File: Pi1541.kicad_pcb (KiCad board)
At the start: 2 copper layers, 56.5 x 65 mm, 25 parts, among them J2 DIN, J3 OLED, Q1 BSS138, Q2 BSS138, Q3 BSS138, Q4 BSS138, U1 74LS06

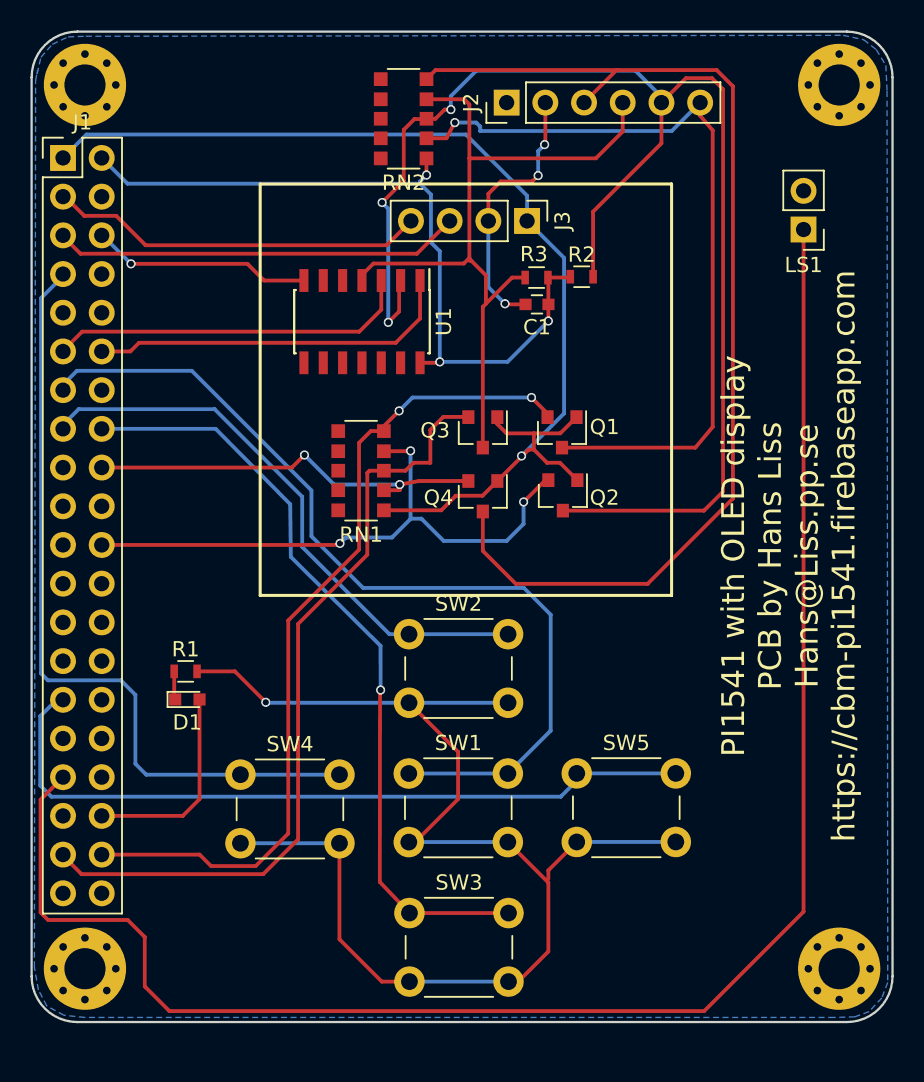
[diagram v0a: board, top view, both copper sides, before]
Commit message: Rearranged everything to correct errors Changed the buzzer footprint Replaced resistor nets with individual resistors
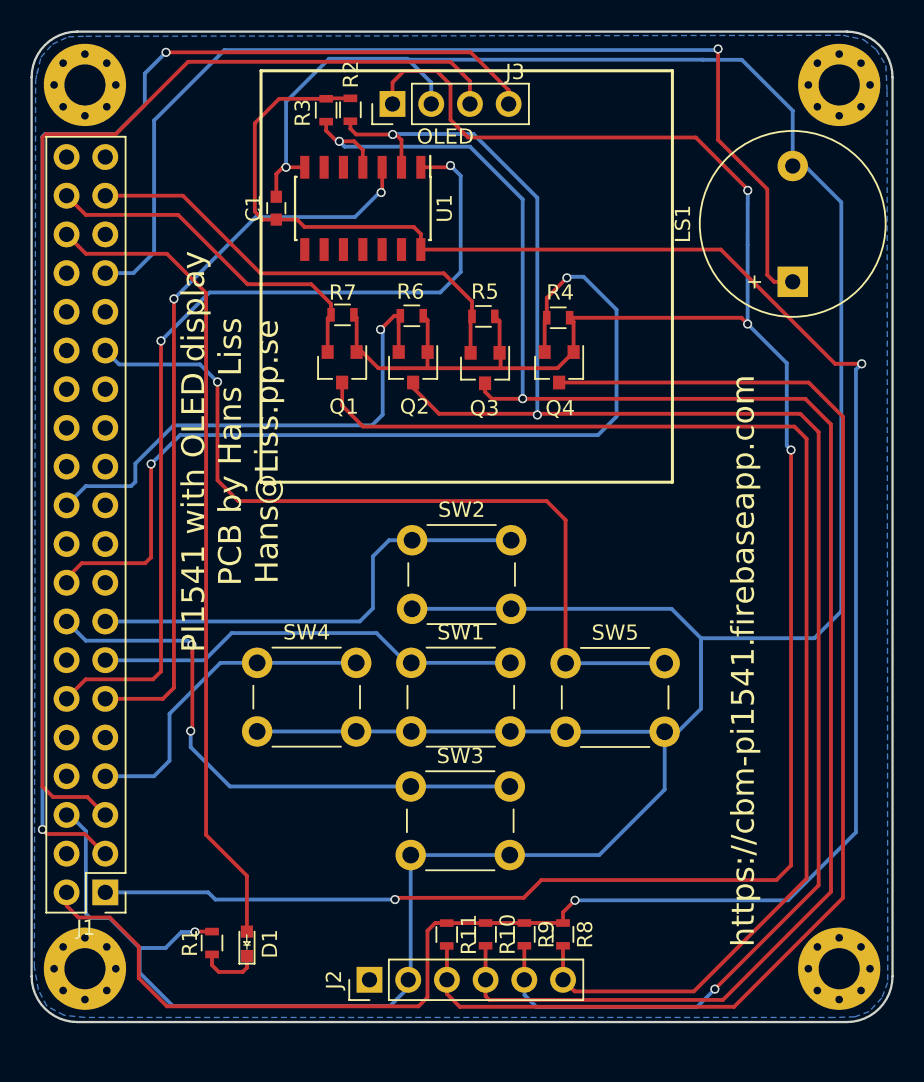
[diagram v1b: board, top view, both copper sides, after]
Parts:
- removed RN1, RN2: 10k, Resistors_SMD:R_Array_Convex_5x1206
- added R10: 10k, Resistors_SMD:R_0603, F.Cu at (114.8, 139.2)
- added R11: 10k, Resistors_SMD:R_0603, F.Cu at (112.2, 139.3)
- added R4: 10k, Resistors_SMD:R_0603, F.Cu at (119.6, 98.8)
- added R5: 10k, Resistors_SMD:R_0603, F.Cu at (114.7, 98.7)
- added R6: 10k, Resistors_SMD:R_0603, F.Cu at (110.0, 98.7)
- added R7: 10k, Resistors_SMD:R_0603, F.Cu at (105.4, 98.6)
- added R8: 10k, Resistors_SMD:R_0603, F.Cu at (119.9, 139.2)
- added R9: 10k, Resistors_SMD:R_0603, F.Cu at (117.3, 139.2)
- J1: value (none) -> Raspberry_Pi_2_3
- LS1: value Buzzer -> Speaker_Crystal; footprint Pin_Headers:Pin_Header_Straight_1x02_Pitch2.54mm -> Buzzers_Beepers:Buzzer_12x9.5RM7.6
- SW1, SW2, SW3, SW4, SW5: value (none) -> SW_Push
- moved J2 58.3 mm to (107.2, 142.2)
- moved J1 48.3 mm to (89.8, 136.5), turned to 180 degrees
- moved R2 18.7 mm to (105.9, 85.1), turned to 270 degrees
- moved C1 18.2 mm to (101.1, 91.6), turned to 90 degrees
- moved R1 17.9 mm to (96.8, 139.8), turned to 90 degrees
- moved R3 17.6 mm to (104.3, 85.2), turned to 270 degrees
- moved D1 16.5 mm to (99.1, 139.9), turned to 90 degrees
- moved Q1 15.0 mm to (105.4, 102.0)
- moved Q2 12.9 mm to (110.0, 102.0)
- moved J3 11.7 mm to (108.7, 84.7), turned to 90 degrees
- moved Q4 9.83 mm to (119.6, 102.0)
- moved SW3 8.31 mm to (109.9, 129.5)
- moved U1 7.43 mm to (106.7, 91.6)
- moved SW4 7.42 mm to (99.8, 121.4)
- moved SW5 7.27 mm to (120.0, 121.4)
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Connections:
- J1 pad 10: Net-(J1-Pad10) -> (no net)
- J1 pad 14: Net-(J1-Pad14) -> (no net)
- J1 pad 17: Net-(J1-Pad17) -> (no net)
- J1 pad 19: Net-(J1-Pad19) -> (no net)
- J1 pad 20: Net-(J1-Pad20) -> (no net)
- J1 pad 21: Net-(J1-Pad21) -> (no net)
- J1 pad 23: Net-(J1-Pad23) -> (no net)
- J1 pad 24: Net-(J1-Pad24) -> (no net)
- J1 pad 25: Net-(J1-Pad25) -> (no net)
- J1 pad 26: Net-(J1-Pad26) -> (no net)
- J1 pad 27: Net-(J1-Pad27) -> (no net)
- J1 pad 28: Net-(J1-Pad28) -> (no net)
- J1 pad 30: Net-(J1-Pad30) -> (no net)
- J1 pad 31: Net-(J1-Pad31) -> (no net)
- J1 pad 32: Net-(J1-Pad32) -> (no net)
- J1 pad 34: Net-(J1-Pad34) -> (no net)
- J1 pad 35: Net-(J1-Pad35) -> (no net)
- J1 pad 39: Net-(J1-Pad39) -> (no net)
- J1 pad 4: Net-(J1-Pad4) -> (no net)
- J1 pad 40: Net-(J1-Pad40) -> (no net)
- J1 pad 8: Net-(J1-Pad8) -> (no net)
- J1 pad 9: Net-(J1-Pad9) -> (no net)
- J2 pad 1: Net-(J2-Pad1) -> (no net)
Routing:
- net +5V: track 49.6 -> 152.7 mm, vias 3 -> 2
- net GND: track 118.6 -> 216.2 mm, vias 5 -> 2
- net +3V3: track 74.8 -> 160.2 mm, vias 1 -> 4
- net /CLK_H: track 49.9 -> 115.6 mm, vias 0 -> 2
- net /SDA: track 24.8 -> 86.3 mm, vias 0 -> 2
- net /SCL: track 26.8 -> 79.6 mm
- net Net-(J1-Pad33): track 111.6 -> 69.6 mm, vias 0 -> 1
- net Net-(D1-Pad2): track 13.4 -> 53.8 mm
- net /DATA_L: track 24.3 -> 59.4 mm, vias 0 -> 2
- net Net-(J1-Pad18): track 27.1 -> 61.0 mm
- net Net-(J1-Pad38): track 55.5 -> 23.8 mm, vias 2 -> 0
- net /RST: track 51.9 -> 83.4 mm, vias 1 -> 0
- net Net-(J1-Pad13): track 59.3 -> 28.1 mm
- net Net-(J1-Pad7): track 51.8 -> 21.4 mm
- net /CLK_L: track 24.0 -> 48.5 mm, vias 0 -> 2
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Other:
- board text added: "OLED"
- board text added: "PI1541 with OLED display PCB by Hans Liss Hans@Liss.pp.se"
- board text added: "https://cbm-pi1541.firebaseapp.com"
- board text removed: "PI1541 with OLED display PCB by Hans Liss Hans@Liss.pp.se https://cbm-pi1541.firebaseapp.com"

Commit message: Replaced the SIL pin header for the DIN connector with a DIL pin header
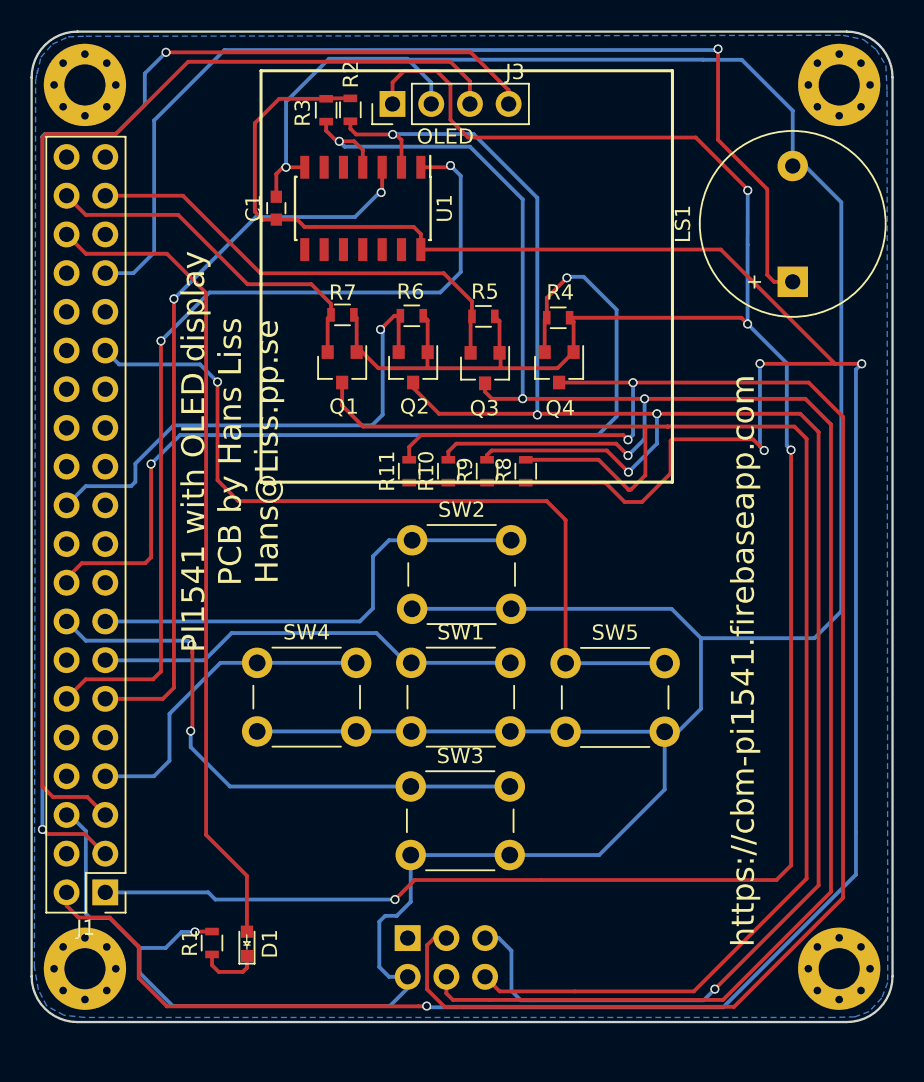
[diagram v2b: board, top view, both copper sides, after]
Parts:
- J2: footprint Pin_Headers:Pin_Header_Straight_1x06_Pitch2.54mm -> Pin_Headers:Pin_Header_Straight_2x03_Pitch2.54mm; moved to B.Cu
- moved R11 30.5 mm to (109.8, 108.8), turned to 90 degrees
- moved R9 30.5 mm to (114.9, 108.8), turned to 90 degrees
- moved R8 30.5 mm to (117.4, 108.8), turned to 90 degrees
- moved R10 30.5 mm to (112.3, 108.8), turned to 90 degrees
- moved J2 3.71 mm to (109.7, 139.5), turned to 270 degrees
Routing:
- net +5V: track 152.7 -> 189.2 mm, vias 2 -> 4
- net /ATN: track 83.6 -> 105.9 mm, vias 0 -> 2
- net /CLK_H: track 115.6 -> 133.1 mm, vias 2 -> 4
- net /DATA_H: track 115.9 -> 132.9 mm, vias 3 -> 5
- net /RST: track 83.4 -> 98.7 mm
- net GND: track 216.2 -> 218.7 mm
